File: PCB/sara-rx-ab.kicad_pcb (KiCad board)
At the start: 4 copper layers, 82.4 x 53.3 mm, 129 parts, among them J1 SOLAR PV, J2 Bridge, J3 FTSH-105-01, J4 Bridge, J7 SMO-1512, J8 Bridge, P1 Power, P2 Analog, P4 Digital, P5 CONN_01X01, P6 CONN_01X01, P7 CONN_01X01, P8 CONN_01X01, Q2 MUN5214DW1T1G, Q3 MUN5214DW1T1G, SW1 PWR_ON, SW2 KMR2, SW3 KMR2, U1 USBLC6-2SC6, U10 NINA-B3, U11 SHT20, U2 USBLC6-2SC6, U3 TXS0108EPWR, U4 USBLC6-2SC6, U5 HT42B534-MSOP, U6 AEM10941, U7 TP4054, U8 TPS61021A, U9 SARA-R511M

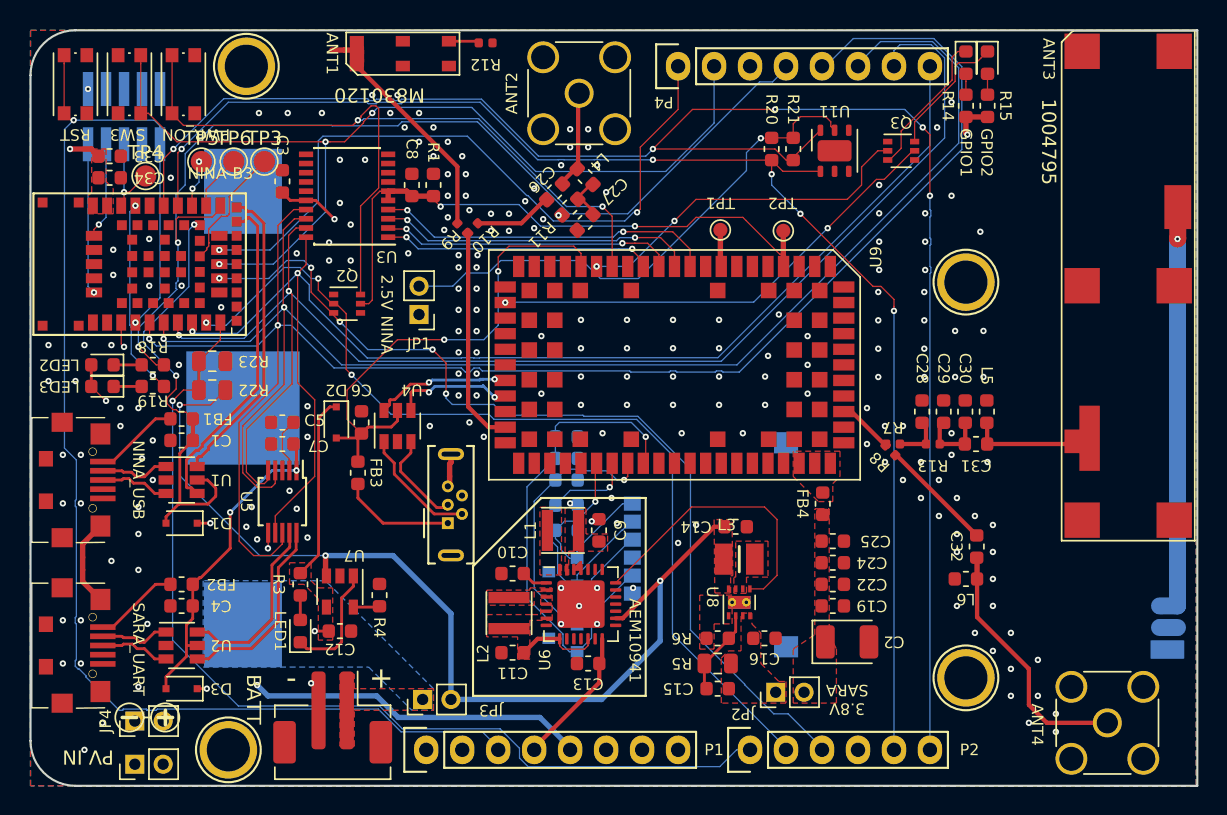
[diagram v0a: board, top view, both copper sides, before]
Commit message: PCB Rev0.1.0 Fix level shifter and silk
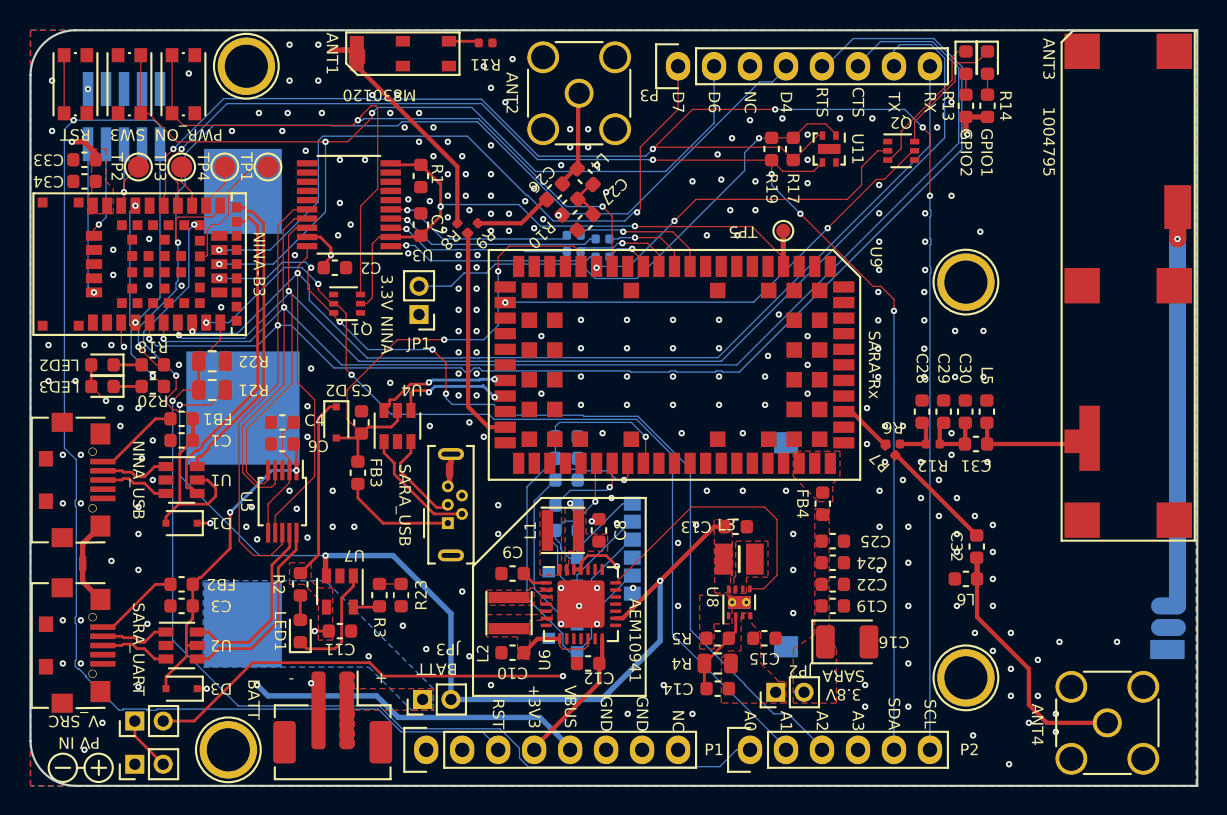
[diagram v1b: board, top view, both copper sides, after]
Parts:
- removed the P4 at (156.7, 75.6)
- removed the R20 at (163.3, 81.4)
- removed the TP1 at (159.7, 87.1)
- removed the TP4 at (119.1, 83.3)
- added P3: Digital, Socket_Arduino_Uno:Socket_Strip_Arduino_1x08, F.Cu at (156.7, 75.6)
- added R19: 10K, Resistor_SMD:R_0603_1608Metric, F.Cu at (163.3, 81.4)
- added R23: 10K, Resistor_SMD:R_0603_1608Metric, F.Cu at (137.2, 112.9)
- added R24: 0R, Resistor_SMD:R_0402_1005Metric, B.Cu at (149.4, 88.6)
- added R25: 0R, Resistor_SMD:R_0402_1005Metric, B.Cu at (151.4, 89.0)
- added R26: 0R, Resistor_SMD:R_0402_1005Metric, B.Cu at (149.4, 87.5)
- added R27: 0R, Resistor_SMD:R_0402_1005Metric, B.Cu at (151.4, 87.8)
- added TP2: TestPoint, TestPoint:TestPoint_Pad_D1.5mm, F.Cu at (118.6, 82.7)
- U11: value SHT20 -> SHTC3; footprint Package_DFN_QFN:DFN-6-1EP_3x3mm_P1mm_EP1.5x2.4mm -> Package_DFN_QFN:AMS_QFN-4-1EP_2x2mm_P0.95mm_EP0.7x1.6mm
- U3: value TXS0108EPWR -> TXS0108EPW; footprint Package_SO:SSOP-20_4.4x6.5mm_P0.65mm -> Package_SO:TSSOP-20_4.4x6.5mm_P0.65mm
- U9: value SARA-R511M -> SARA-Rx
- moved C2 7.14 mm to (132.5, 89.8), turned to 0 degrees
- moved REF** 5.89 mm to (113.3, 125.1) (x2)
- moved C7 2.87 mm to (138.6, 86.7)
- moved C34 1.80 mm to (114.8, 83.7), turned to 180 degrees
- moved C33 1.80 mm to (114.8, 82.2), turned to 180 degrees
- moved TP3 1.45 mm to (121.7, 82.7)
- moved R1 1.09 mm to (138.6, 83.3), turned to 90 degrees
- moved TP4 0.74 mm to (124.7, 82.7)
- moved U3 0.65 mm to (133.5, 85.3)
- moved TP1 0.46 mm to (127.8, 82.7)
- moved U11 0.40 mm to (167.4, 81.4), turned to 270 degrees
- renumbered C11 to C10, C12 to C11, C13 to C12, C14 to C13, C15 to C14, C16 to C15, C2 to C16, C3 to C2, C4 to C3, C5 to C4, C6 to C5, C7 to C6, C8 to C7, C9 to C8, C10 to C9, GPIO2 to GPIO1, GPIO1 to GPIO2, J7 to J5, J8 to J6, P5 to P4, P6 to P5, P7 to P6, P8 to P7, Q2 to Q1, Q3 to Q2, R11 to R10, R12 to R11, R13 to R12, R14 to R13, R15 to R14, R16 to R15, R17 to R16, R21 to R17, R3 to R2, R19 to R20, R22 to R21, R23 to R22, R4 to R3, R5 to R4, R6 to R5, R7 to R6, R8 to R7, R9 to R8, R10 to R9, TP3 to TP1, TP5 to TP3, TP6 to TP4, TP2 to TP5
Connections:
- net /SARA-R5/ANT_EXT renamed /SARA-Rx/ANT_EXT
- net /SARA-R5/ANT_INT renamed /SARA-Rx/ANT_INT
- net /SARA-R5/GNSS_EXT renamed /SARA-Rx/GNSS_EXT
- net /SARA-R5/GNSS_INT renamed /SARA-Rx/GNSS_INT
- net /SARA-R5/GPIO1 renamed /SARA-Rx/GPIO1
- net /SARA-R5/GPIO2 renamed /SARA-Rx/GPIO2
- net /SARA-R5/PWR_ON renamed /SARA-Rx/PWR_ON
- net /SARA-R5/SIM_CLK renamed /SARA-Rx/SIM_CLK
- net /SARA-R5/SIM_IO renamed /SARA-Rx/SIM_IO
- net /SARA-R5/SIM_RST renamed /SARA-Rx/SIM_RST
- net /SARA-R5/VSIM renamed /SARA-Rx/VSIM
- C12 pad 1: +2V5 -> +3V3
- C2 pad 1: +2V5 -> +3V3
- C33 pad 1: +2V5_NINA -> +3V3_NINA
- C34 pad 1: +2V5_NINA -> +3V3_NINA
- C4 pad 2: Net-(C5-Pad2) -> Net-(C4-Pad2)
- J3 pad 1: +2V5 -> +3V3
- JP1 pad 1: +2V5 -> +3V3
- JP1 pad 2: +2V5_NINA -> +3V3_NINA
- LED2 pad 2: +2V5_NINA -> +3V3_NINA
- LED3 pad 2: +2V5_NINA -> +3V3_NINA
- P1 pad 4: +2V5 -> +3V3
- R17 pad 1: +2V5_NINA -> +3V3_NINA
- R3 pad 2: GND -> Net-(R23-Pad1)
- U10 pad 10: +2V5_NINA -> +3V3_NINA
- U10 pad 9: +2V5_NINA -> +3V3_NINA
- U11 pad 1: SDA -> +3V3_NINA
- U11 pad 2: GND -> SCL
- U11 pad 3: (no net) -> SDA
- U11 pad 4: (no net) -> GND
- U11 pad 5: +2V5_NINA -> (no net)
- U3 pad 1: /SARA-R5/SARA_RX -> /SARA-Rx/SARA_RX
- U3 pad 10: (no net) -> +1V8
- U3 pad 11: (no net) -> GND
- U3 pad 15: GND -> (no net)
- U3 pad 16: +2V5 -> MCU_RTS
- U3 pad 17: MCU_RTS -> MCU_CTS
- U3 pad 18: MCU_CTS -> MCU_TX
- U3 pad 19: MCU_TX -> +3V3
- U3 pad 2: /SARA-R5/SARA_TX -> +1V8
- U3 pad 3: /SARA-R5/SARA_CTS -> /SARA-Rx/SARA_TX
- U3 pad 4: /SARA-R5/SARA_RTS -> /SARA-Rx/SARA_CTS
- U3 pad 5: +1V8 -> /SARA-Rx/SARA_RTS
- U3 pad 6: +1V8 -> (no net)
- U5 pad 2: Net-(C5-Pad2) -> Net-(C4-Pad2)
- U5 pad 6: +2V5 -> Net-(C4-Pad2)
- U6 pad 14: +2V5 -> +3V3
- U9 pad 10: /SARA-R5/SARA_RTS -> Net-(R26-Pad2)
- U9 pad 11: /SARA-R5/SARA_CTS -> Net-(R27-Pad2)
- U9 pad 12: /SARA-R5/SARA_TX -> Net-(R24-Pad2)
- U9 pad 13: /SARA-R5/SARA_RX -> Net-(R25-Pad2)
- U9 pad 8: Net-(TP1-Pad1) -> (no net)
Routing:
- net +2V5_NINA: track 90.5 -> 0.00 mm, vias 3 -> 0
- net +3V3_NINA: track 0.00 -> 89.1 mm, vias 0 -> 3
- net +2V5: track 49.1 -> 0.00 mm, vias 3 -> 0
- net +3V3: track 0.00 -> 48.9 mm, vias 0 -> 2
- net +V_PV: track 1.83 -> 43.7 mm, vias 0 -> 2
- net /SARA-R5/SARA_RTS: track 24.0 -> 0.00 mm, vias 2 -> 0
- net /SARA-R5/SARA_CTS: track 22.4 -> 0.00 mm, vias 2 -> 0
- net /SARA-R5/SARA_TX: track 20.8 -> 0.00 mm, vias 2 -> 0
- net /SARA-R5/SARA_RX: track 19.1 -> 0.00 mm, vias 2 -> 0
- net /SARA-Rx/SARA_CTS: track 0.00 -> 15.6 mm, vias 0 -> 1
- net /SARA-Rx/SARA_RX: track 0.00 -> 15.2 mm, vias 0 -> 1
- net /SARA-Rx/SARA_RTS: track 0.00 -> 13.6 mm, vias 0 -> 1
- net /SARA-Rx/SARA_TX: track 0.00 -> 13.3 mm, vias 0 -> 1
- net Net-(R26-Pad2): track 0.00 -> 9.67 mm, vias 0 -> 1
- net Net-(C4-Pad2): track 0.00 -> 8.96 mm
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- added copper zone on In2.Cu, net +3V3
- added copper zone on F.Cu, net +3V3_NINA
- removed copper zone on In2.Cu, net +2V5
- removed copper zone on F.Cu, net +2V5_NINA
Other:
- board text added: "+3V3"
- board text added: "202004_REV0.1"
- board text added: "3.3V NINA"
- board text added: "A0"
- board text added: "A1"
- board text added: "A2"
- board text added: "A3"
- board text added: "CTS"
- board text added: "D4"
- board text added: "D6"
- board text added: "D7"
- board text added: "GND"
- board text added: "NC"
- board text added: "RST"
- board text added: "RTS"
- board text added: "RX"
- board text added: "SARA-Rx"
- board text added: "SARA_USB"
- board text added: "SCL"
- board text added: "SDA"
- board text added: "TX"
- board text added: "VBUS"
- board text added: "V_SRC"
- board text removed: "2.5V NINA"
- board text removed: "201910_REV0.0.1"
